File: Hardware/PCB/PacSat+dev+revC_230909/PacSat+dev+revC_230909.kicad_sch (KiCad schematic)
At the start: 4 parts

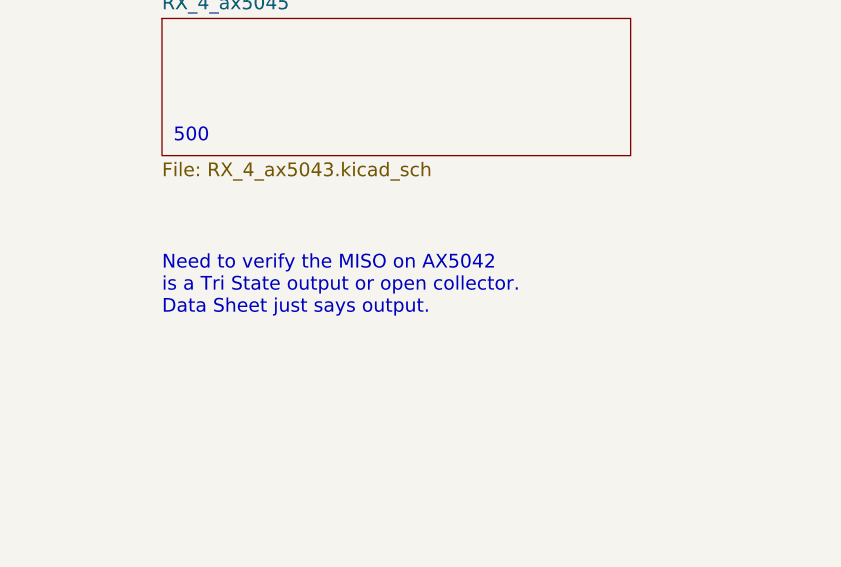
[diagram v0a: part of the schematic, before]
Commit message: Changed schematic to add Select lines for each AX5043 on the CPU.
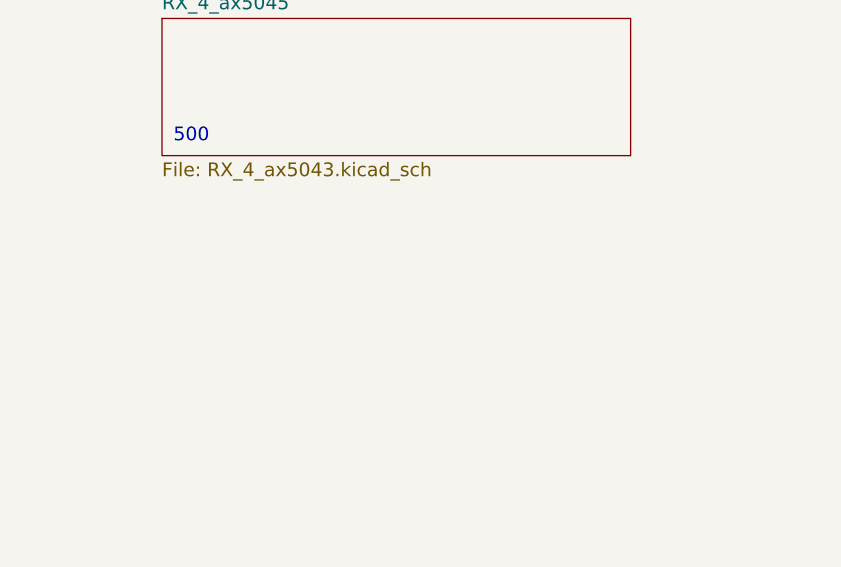
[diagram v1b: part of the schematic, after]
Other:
- note removed: "Need to verify the MISO on AX5042 is a Tri State output or open collector. Data Sheet just says output."
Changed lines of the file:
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@@
     (effects (font (size 1.524 1.524)) (justify left bottom))
-  )
-  (text "Need to verify the MISO on AX5042\nis a Tri State output or open collector.\nData Sheet just says output."
-    (at 210.82 156.21 0)
-    (effects (font (size 1.524 1.524) (color 255 0 0 1)) (justify left bottom))
   )
   (text "800" (at 271.78 88.9 0)
@@
     (pin "1")
     (instances
-      (project "pACsAT_dEV_rEVc_230907"
+      (project "PacSat+dev+revC_230909"
         (path "/cc9f42d2-6985-41ac-acab-5ab7b01c5b38"
           (reference "H101") (unit 1)
@@
     (pin "1")
     (instances
-      (project "pACsAT_dEV_rEVc_230907"
+      (project "PacSat+dev+revC_230909"
         (path "/cc9f42d2-6985-41ac-acab-5ab7b01c5b38"
           (reference "H102") (unit 1)
@@
     (pin "1")
     (instances
-      (project "pACsAT_dEV_rEVc_230907"
+      (project "PacSat+dev+revC_230909"
         (path "/cc9f42d2-6985-41ac-acab-5ab7b01c5b38"
           (reference "H103") (unit 1)
@@
     (pin "1")
     (instances
-      (project "pACsAT_dEV_rEVc_230907"
+      (project "PacSat+dev+revC_230909"
         (path "/cc9f42d2-6985-41ac-acab-5ab7b01c5b38"
           (reference "H104") (unit 1)
@@
     (pin "1")
     (instances
-      (project "pACsAT_dEV_rEVc_230907"
+      (project "PacSat+dev+revC_230909"
         (path "/cc9f42d2-6985-41ac-acab-5ab7b01c5b38"
           (reference "#PWR0101") (unit 1)
@@
     )
     (instances
-      (project "pACsAT_dEV_rEVc_230907"
+      (project "PacSat+dev+revC_230909"
         (path "/cc9f42d2-6985-41ac-acab-5ab7b01c5b38" (page "6"))
       )
@@
     )
     (instances
-      (project "pACsAT_dEV_rEVc_230907"
+      (project "PacSat+dev+revC_230909"
         (path "/cc9f42d2-6985-41ac-acab-5ab7b01c5b38" (page "8"))
       )
@@
     )
     (instances
-      (project "pACsAT_dEV_rEVc_230907"
+      (project "PacSat+dev+revC_230909"
         (path "/cc9f42d2-6985-41ac-acab-5ab7b01c5b38" (page "5"))
       )
@@
     )
     (instances
-      (project "pACsAT_dEV_rEVc_230907"
+      (project "PacSat+dev+revC_230909"
         (path "/cc9f42d2-6985-41ac-acab-5ab7b01c5b38" (page "15"))
       )
@@
     )
     (instances
-      (project "pACsAT_dEV_rEVc_230907"
+      (project "PacSat+dev+revC_230909"
         (path "/cc9f42d2-6985-41ac-acab-5ab7b01c5b38" (page "7"))
       )
@@
     )
     (instances
-      (project "pACsAT_dEV_rEVc_230907"
+      (project "PacSat+dev+revC_230909"
         (path "/cc9f42d2-6985-41ac-acab-5ab7b01c5b38" (page "17"))
       )
@@
     )
     (instances
-      (project "pACsAT_dEV_rEVc_230907"
+      (project "PacSat+dev+revC_230909"
         (path "/cc9f42d2-6985-41ac-acab-5ab7b01c5b38" (page "9"))
       )
@@
     )
     (instances
-      (project "pACsAT_dEV_rEVc_230907"
+      (project "PacSat+dev+revC_230909"
         (path "/cc9f42d2-6985-41ac-acab-5ab7b01c5b38" (page "2"))
       )
@@
     )
     (instances
-      (project "pACsAT_dEV_rEVc_230907"
+      (project "PacSat+dev+revC_230909"
         (path "/cc9f42d2-6985-41ac-acab-5ab7b01c5b38" (page "4"))
       )
@@
     )
     (instances
-      (project "pACsAT_dEV_rEVc_230907"
+      (project "PacSat+dev+revC_230909"
         (path "/cc9f42d2-6985-41ac-acab-5ab7b01c5b38" (page "12"))
       )
@@
     )
     (instances
-      (project "pACsAT_dEV_rEVc_230907"
+      (project "PacSat+dev+revC_230909"
         (path "/cc9f42d2-6985-41ac-acab-5ab7b01c5b38" (page "13"))
       )
@@
     )
     (instances
-      (project "pACsAT_dEV_rEVc_230907"
+      (project "PacSat+dev+revC_230909"
         (path "/cc9f42d2-6985-41ac-acab-5ab7b01c5b38" (page "14"))
       )
@@
     )
     (instances
-      (project "pACsAT_dEV_rEVc_230907"
+      (project "PacSat+dev+revC_230909"
         (path "/cc9f42d2-6985-41ac-acab-5ab7b01c5b38" (page "10"))
       )
@@
     )
     (instances
-      (project "pACsAT_dEV_rEVc_230907"
+      (project "PacSat+dev+revC_230909"
         (path "/cc9f42d2-6985-41ac-acab-5ab7b01c5b38" (page "11"))
       )
